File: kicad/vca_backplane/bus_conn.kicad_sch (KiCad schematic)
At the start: 1 part, among them J6 Conn_02x20_Odd_Even

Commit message: v0.2 of backplane submitted to jlcpcb
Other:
- title: (none) -> Zoxnoxious Backplane and VCA
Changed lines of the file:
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@@
   (paper "A4")
   (title_block
+    (title "Zoxnoxious Backplane and VCA")
+    (date "2022-08-28")
+    (rev "0.2")
     (company "Zoxnoxious Engineering")
   )

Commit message: moved 2x20 5mm back
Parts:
- J6: footprint Connector_PinSocket_2.54mm:PinSocket_2x20_P2.54mm_SullinsPolarized -> project_footprints:PinSocket_2x20_P2.54mm_SullinsPolarized
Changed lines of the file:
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@@
     (property "Reference" "J6" (id 0) (at 71.12 19.8882 0))
     (property "Value" "Conn_02x20_Odd_Even" (id 1) (at 71.12 22.1996 0))
-    (property "Footprint" "Connector_PinSocket_2.54mm:PinSocket_2x20_P2.54mm_SullinsPolarized" (id 2) (at 69.85 48.26 0)
+    (property "Footprint" "project_footprints:PinSocket_2x20_P2.54mm_SullinsPolarized" (id 2) (at 69.85 48.26 0)
       (effects (font (size 1.27 1.27)) hide)
     )

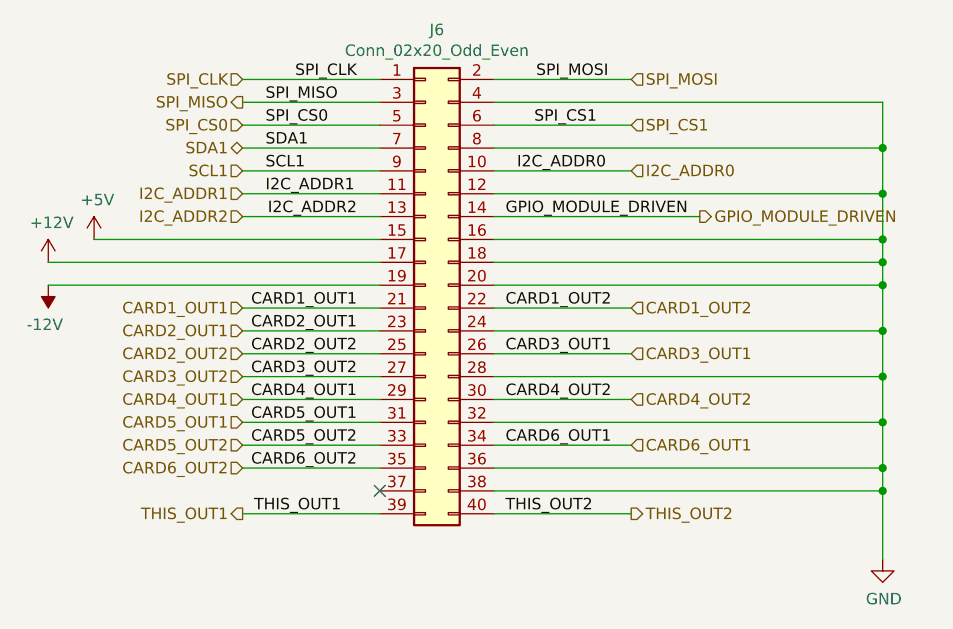
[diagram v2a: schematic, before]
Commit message: schematic for backplane v0.3: change Pi GPIOs for SPI; switch output jacks; add external input
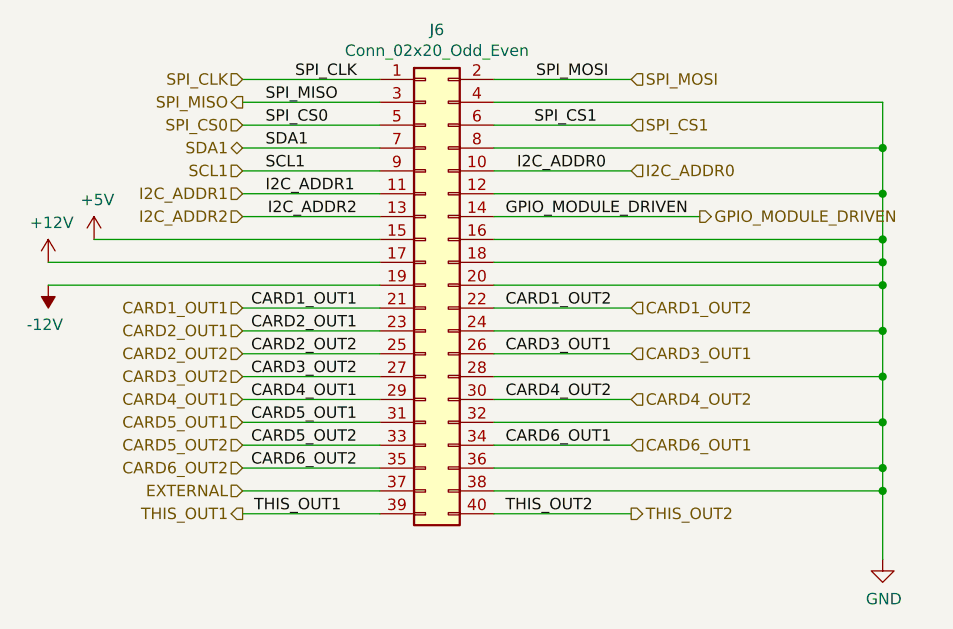
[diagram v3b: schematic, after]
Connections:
- net EXTERNAL: now reaches J6.37 (Pin_37)
- no-connect marks 1 -> 0

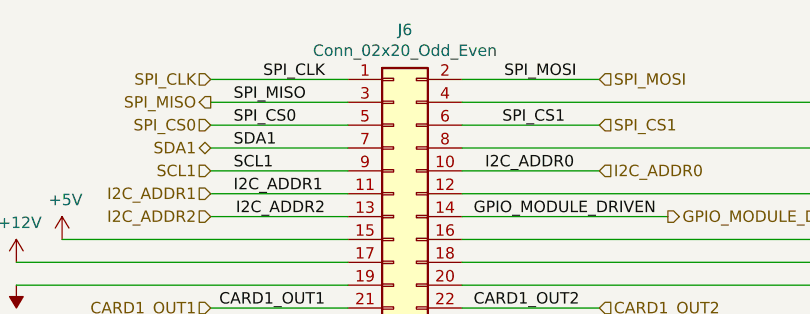
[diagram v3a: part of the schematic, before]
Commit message: geographically reorientated from pcb
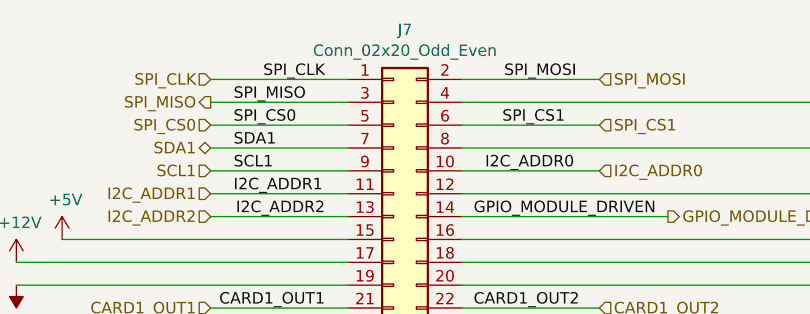
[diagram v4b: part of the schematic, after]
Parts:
- renumbered J6 to J7
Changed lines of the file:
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@@
   (symbol (lib_id "Connector_Generic:Conn_02x20_Odd_Even") (at 69.85 48.26 0) (unit 1)
     (in_bom yes) (on_board yes) (dnp no)
-    (property "Reference" "J6" (at 71.12 19.8882 0)
+    (property "Reference" "J7" (at 71.12 19.8882 0)
       (effects (font (size 1.27 1.27)))
     )
@@
       (project "vca_backplane"
         (path "/bdbd6910-8f28-459f-89ba-e6dd447d59a9/00000000-0000-0000-0000-0000625442ef"
-          (reference "J6") (unit 1)
+          (reference "J7") (unit 1)
         )
         (path "/bdbd6910-8f28-459f-89ba-e6dd447d59a9/00000000-0000-0000-0000-000062525dc6"
@@
         )
         (path "/bdbd6910-8f28-459f-89ba-e6dd447d59a9/00000000-0000-0000-0000-000062544309"
-          (reference "J7") (unit 1)
+          (reference "J10") (unit 1)
         )
         (path "/bdbd6910-8f28-459f-89ba-e6dd447d59a9/00000000-0000-0000-0000-00006252a02b"
-          (reference "J4") (unit 1)
+          (reference "J2") (unit 1)
         )
         (path "/bdbd6910-8f28-459f-89ba-e6dd447d59a9/00000000-0000-0000-0000-000062544323"
-          (reference "J8") (unit 1)
+          (reference "J11") (unit 1)
         )
         (path "/bdbd6910-8f28-459f-89ba-e6dd447d59a9/00000000-0000-0000-0000-00006252a045"
